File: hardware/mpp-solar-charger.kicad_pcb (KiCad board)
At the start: 2 copper layers, 136 parts, among them J101 Conn_01x04, J102 Conn_01x05, J103 Conn_01x05, Q201 Q_PNP_CBE, Q202 Q_PNP_CBE, Q203 Q_PNP_CBE, Q204 Q_PNP_CBE, Q205 Q_PNP_CBE, Q206 Q_NPN_CBE, Q207 Q_PNP_CBE, Q208 Q_PNP_CBE, Q209 Q_NPN_CBE, Q301 IRFZ48N, Q302 IRFZ48N, Q303 Q_PNP_CBE, Q304 BD135, Q305 BD136, Q306 Q_NPN_CBE, Q307 Q_PNP_CBE, Q308 Q_PNP_CBE, Q309 Q_NPN_CBE, Q310 Q_PNP_CBE, Q311 Q_PNP_CBE, Q312 Q_NPN_CBE, Q313 Q_NPN_CBE, U201 LP2950L-5.0, U202 LM324, U203 LM393

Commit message: Initial layout work
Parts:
- removed D305: D, Diodes_ThroughHole:D_DO-35_SOD27_P7.62mm_Horizontal
- D302: value D_Schottky -> MBR4045PT; footprint TO_SOT_Packages_THT:TO-220-2_Vertical -> TO_SOT_Packages_THT:TO-247_TO-3P_Vertical
- D303: value D_Schottky -> D_Zener; footprint TO_SOT_Packages_THT:TO-220-2_Vertical -> Diodes_ThroughHole:D_DO-41_SOD81_P7.62mm_Horizontal
- D304: value D_Zener -> D; footprint Diodes_ThroughHole:D_DO-41_SOD81_P7.62mm_Horizontal -> Diodes_ThroughHole:D_DO-35_SOD27_P7.62mm_Horizontal
- R306, R307: moved to B.Cu
- moved C301 131.7 mm to (278.8, 124.5), turned to 180 degrees
- moved C304 126.5 mm to (275.0, 104.1), turned to 270 degrees
- moved C313 117.7 mm to (262.9, 132.7), turned to 90 degrees
- moved Q209 115.7 mm to (36.0, 78.0)
- moved C212 114.7 mm to (34.0, 111.0)
- moved C211 113.9 mm to (36.0, 87.0)
- moved C205 113.5 mm to (38.0, 131.0)
- moved C208 112.0 mm to (37.0, 94.0)
- moved C302 111.6 mm to (259.7, 113.7), turned to 270 degrees
- moved Q206 111.5 mm to (38.0, 120.0)
- moved C306 111.2 mm to (259.7, 106.7)
- moved C207 109.5 mm to (39.0, 102.0)
- moved R244 108.7 mm to (53.0, 157.0)
- moved Q208 108.6 mm to (45.0, 72.0)
- moved R245 107.8 mm to (57.0, 162.0)
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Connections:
- D302 pad 1: Net-(C307-Pad2) -> GND
- D302 pad 2: GND -> Net-(C307-Pad2)
- D303 pad 1: Net-(C307-Pad2) -> Net-(D303-Pad1)
- D303 pad 2: GND -> Net-(C307-Pad2)
- D304 pad 1: Net-(D304-Pad1) -> Net-(C307-Pad2)
- D304 pad 2: Net-(C307-Pad2) -> Net-(D304-Pad2)
- Q306 pad 2: Net-(D304-Pad1) -> Net-(D303-Pad1)
- Q307 pad 2: Net-(D304-Pad1) -> Net-(D303-Pad1)
- Q310 pad 1: Net-(D304-Pad1) -> Net-(D303-Pad1)
- Q312 pad 3: Net-(D305-Pad2) -> Net-(D304-Pad2)
- Q313 pad 3: Net-(D305-Pad2) -> Net-(D304-Pad2)
- R308 pad 1: Net-(D304-Pad1) -> Net-(D303-Pad1)
- R312 pad 1: Net-(D304-Pad1) -> Net-(D303-Pad1)
- U202 pad 11: (no net) -> Net-(U202-Pad11)
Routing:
- net /Controller/VBAT: track 0.00 -> 70.1 mm
- net GND: track 0.00 -> 20.3 mm
- net Net-(L301-Pad2): track 0.00 -> 19.0 mm
- net Net-(Q303-Pad2): track 0.00 -> 13.4 mm
- net Net-(C309-Pad1): track 0.00 -> 10.3 mm
- net Net-(Q308-Pad3): track 0.00 -> 10.2 mm
- net /Controller/USENSE: track 0.00 -> 6.24 mm
- net Net-(Q303-Pad3): track 0.00 -> 3.59 mm
- net /Controller/UREF: track 0.00 -> 2.80 mm

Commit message: Layout work for power stage
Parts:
- moved Q209 228.3 mm to (264.3, 80.0), turned to 180 degrees
- moved U201 218.8 mm to (259.3, 130.8), turned to 180 degrees
- moved R244 215.4 mm to (267.8, 140.8)
- moved R237 215.2 mm to (267.8, 145.6)
- moved R242 214.8 mm to (267.8, 148.4)
- moved R236 213.0 mm to (267.8, 151.6)
- moved R246 200.1 mm to (257.0, 84.4)
- moved D304 189.8 mm to (263.0, 66.6), turned to 180 degrees
- moved U203 189.1 mm to (257.2, 140.7)
- moved C201 183.5 mm to (252.4, 132.6), turned to 90 degrees
- moved D207 175.0 mm to (267.8, 143.2)
- moved D201 174.0 mm to (251.0, 125.8)
- moved C202 172.9 mm to (263.8, 132.6), turned to 90 degrees
- moved R201 160.9 mm to (240.4, 125.4)
- moved Q312 103.2 mm to (250.2, 66.0)
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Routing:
- net GND: track 20.3 -> 215.1 mm, vias 0 -> 2
- net Net-(C307-Pad2): track 0.00 -> 157.6 mm, vias 0 -> 4
- net /Power-Stage/VSOLAR: track 0.00 -> 94.5 mm
- net Net-(C307-Pad1): track 0.00 -> 58.5 mm
- net Net-(D207-Pad1): track 0.00 -> 56.5 mm
- net /Controller/~SWITCH: track 0.00 -> 54.5 mm
- net Net-(D303-Pad1): track 0.00 -> 42.5 mm
- net Net-(Q301-Pad1): track 0.00 -> 32.1 mm
- net Net-(Q304-Pad3): track 0.00 -> 25.3 mm
- net Net-(Q313-Pad2): track 0.00 -> 20.8 mm
- net Net-(Q304-Pad1): track 0.00 -> 20.6 mm
- net Net-(D304-Pad2): track 0.00 -> 19.0 mm
- net Net-(C201-Pad1): track 0.00 -> 18.4 mm
- net Net-(Q302-Pad1): track 0.00 -> 13.7 mm
- net Net-(Q303-Pad2): track 13.4 -> 0.00 mm
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
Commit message: Layout work
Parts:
- R243: footprint Resistors_ThroughHole:R_Axial_DIN0207_L6.3mm_D2.5mm_P7.62mm_Horizontal -> Resistors_ThroughHole:R_Axial_DIN0207_L6.3mm_D2.5mm_P2.54mm_Vertical
- moved C211 222.5 mm to (255.1, 125.2), turned to 180 degrees
- moved Q206 213.2 mm to (251.1, 128.3), turned to 270 degrees
- moved C209 204.5 mm to (248.5, 112.3)
- moved Q205 203.0 mm to (251.1, 133.7), turned to 270 degrees
- moved Q208 190.0 mm to (225.4, 131.7), turned to 270 degrees
- moved Q204 188.9 mm to (239.0, 134.9), turned to 270 degrees
- moved R231 188.2 mm to (243.3, 124.7), turned to 270 degrees
- moved R230 183.8 mm to (243.3, 134.5), turned to 270 degrees
- moved R229 183.4 mm to (245.4, 111.8), turned to 270 degrees
- moved C207 182.8 mm to (221.8, 106.0), turned to 180 degrees
- moved C204 182.3 mm to (242.2, 101.6), turned to 270 degrees
- moved R228 180.9 mm to (255.4, 127.9), turned to 270 degrees
- moved C206 180.2 mm to (225.0, 99.4), turned to 180 degrees
- moved C208 179.7 mm to (213.4, 128.6), turned to 90 degrees
- moved R222 179.5 mm to (240.7, 140.5), turned to 180 degrees
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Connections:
- U202 pad 1: Net-(C206-Pad2) -> Net-(C210-Pad2)
- U202 pad 10: Net-(R240-Pad1) -> Net-(R220-Pad2)
- U202 pad 11: Net-(U202-Pad11) -> GND
- U202 pad 2: Net-(C207-Pad2) -> Net-(C208-Pad2)
- U202 pad 3: Net-(R220-Pad2) -> Net-(R209-Pad2)
- U202 pad 5: Net-(R209-Pad2) -> Net-(R240-Pad1)
- U202 pad 6: Net-(C208-Pad2) -> Net-(R235-Pad2)
- U202 pad 7: Net-(C210-Pad2) -> Net-(D205-Pad2)
- U202 pad 8: Net-(D205-Pad2) -> Net-(C206-Pad2)
- U202 pad 9: Net-(R235-Pad2) -> Net-(C207-Pad2)
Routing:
- net GND: track 215.1 -> 486.2 mm
- net /Controller/+5V: track 6.22 -> 147.6 mm
- net Net-(C208-Pad2): track 0.00 -> 53.5 mm
- net Net-(C205-Pad1): track 0.00 -> 45.3 mm
- net Net-(R234-Pad2): track 0.00 -> 39.9 mm
- net /Controller/VBAT: track 58.0 -> 93.8 mm
- net Net-(Q203-Pad1): track 0.00 -> 32.1 mm
- net Net-(C210-Pad2): track 0.00 -> 31.2 mm
- net Net-(D207-Pad1): track 56.5 -> 86.5 mm
- net /Controller/UMIN: track 0.00 -> 25.7 mm
- net Net-(Q203-Pad2): track 0.00 -> 25.7 mm
- net Net-(D203-Pad2): track 0.00 -> 25.5 mm, vias 0 -> 2
- net /Controller/UREG: track 0.00 -> 23.9 mm
- net Net-(C206-Pad2): track 0.00 -> 23.6 mm
- net /Controller/USAW: track 0.00 -> 21.3 mm
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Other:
- board outline added: 76.2 x 136.1 mm
- net class Default: clearance 0.2 -> 0.3
- rule trace_clearance: 0.2 -> 0.3

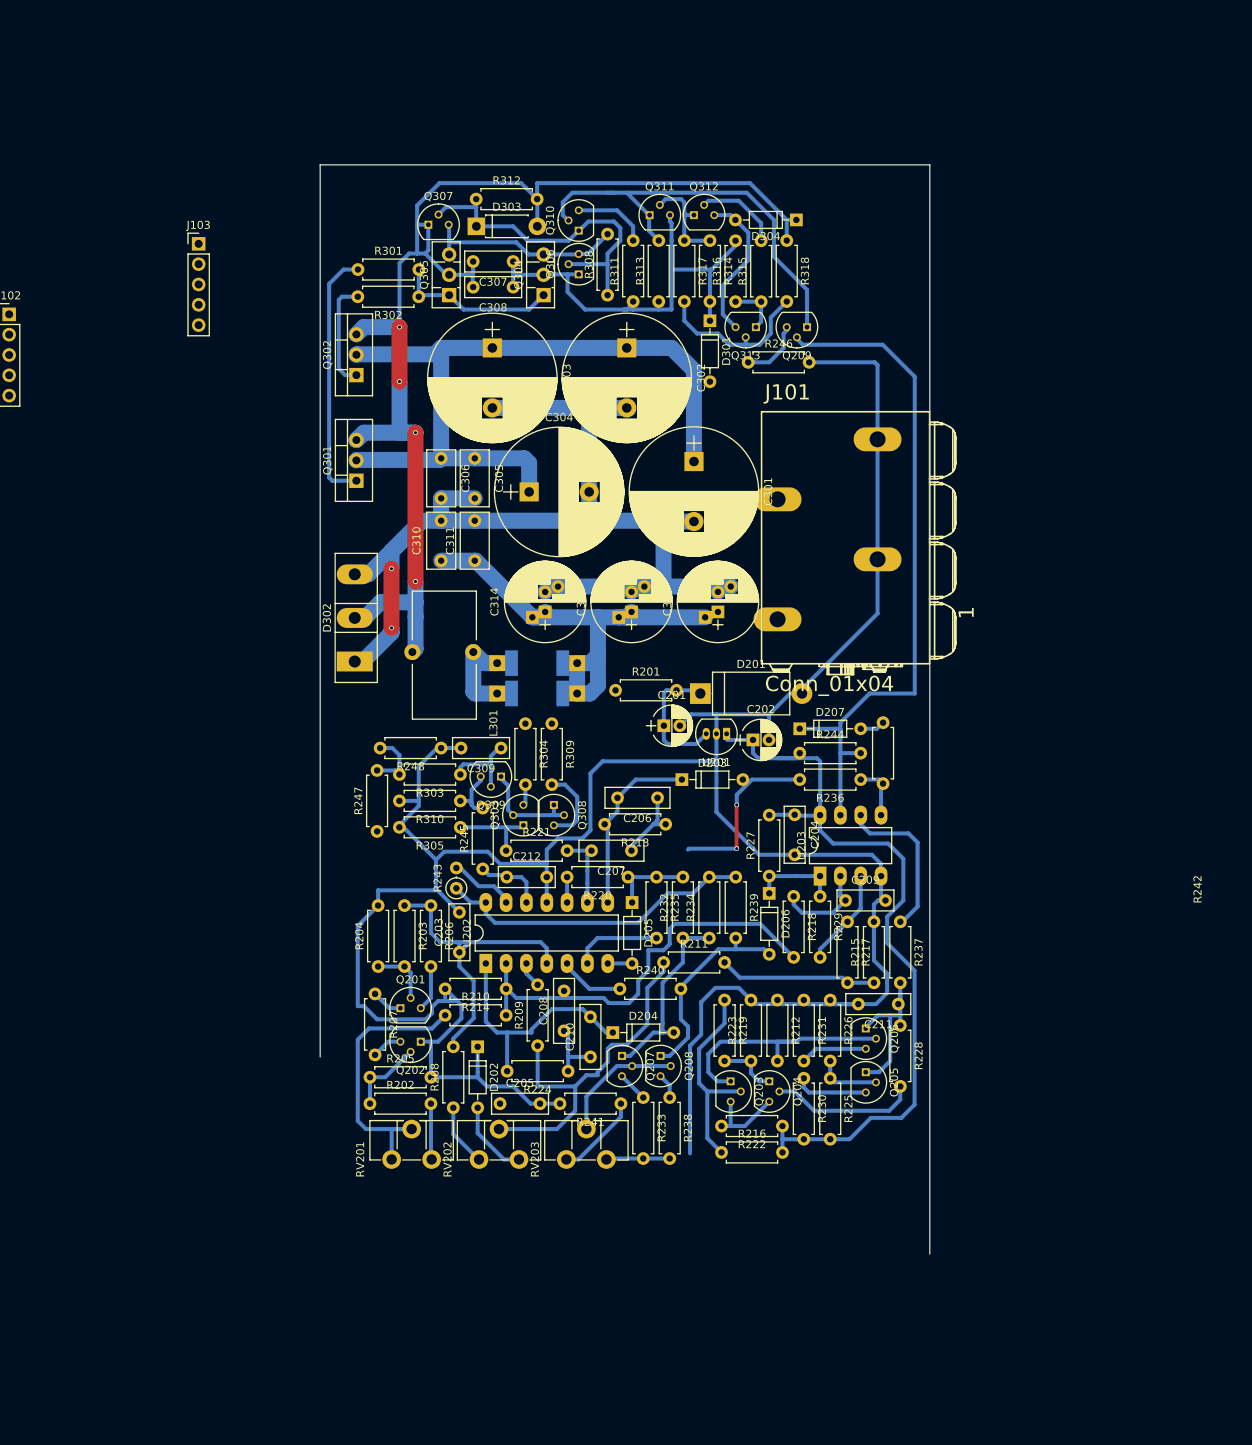
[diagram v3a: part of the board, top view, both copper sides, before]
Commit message: Condense layout
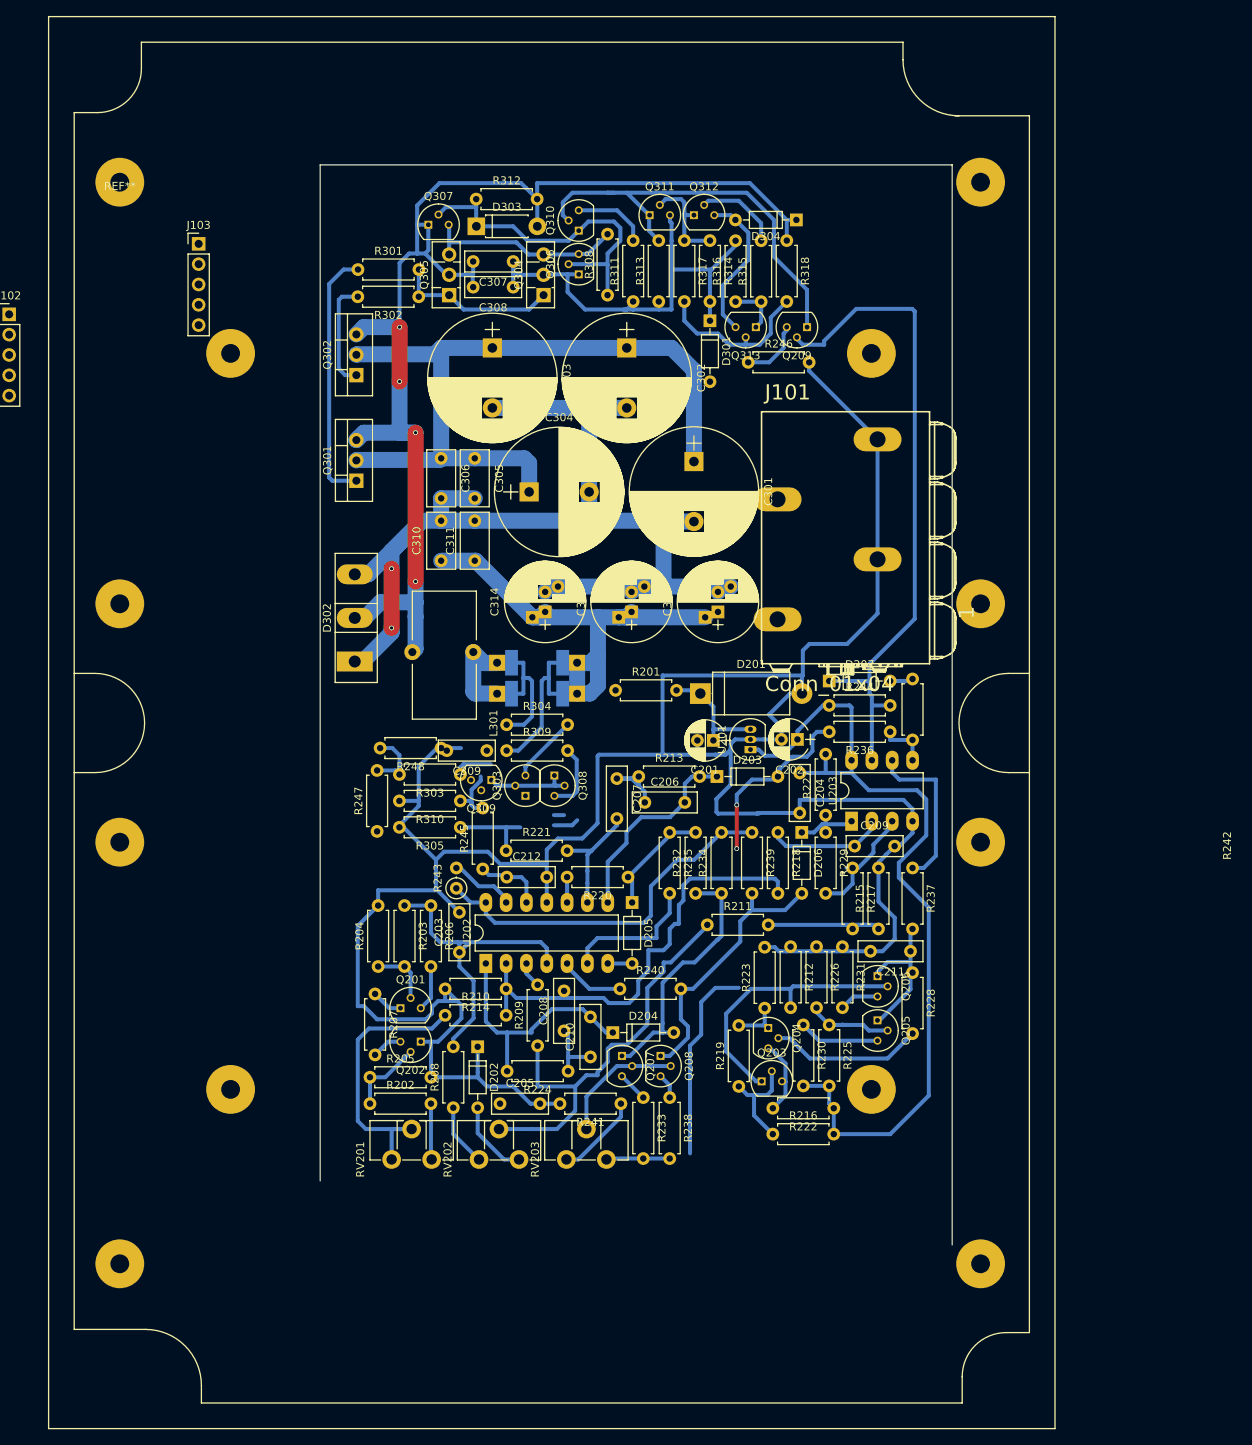
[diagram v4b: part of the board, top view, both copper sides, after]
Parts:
- added REF**: KRADEX_Z74, mpp-solar-charger:KRADEX_Z74, F.Cu at (157.8, 22.5)
- moved R219 10.9 mm to (235.2, 135.5), turned to 90 degrees
- moved R227 10.4 mm to (246.1, 101.6)
- moved C207 9.20 mm to (220.0, 97.0), turned to 270 degrees
- moved D206 8.64 mm to (243.1, 103.8)
- moved R218 8.24 mm to (240.1, 103.8)
- moved R231 8.23 mm to (248.2, 118.0)
- moved R229 8.03 mm to (246.1, 103.8)
- moved U203 7.91 mm to (249.3, 102.4)
- moved R211 7.20 mm to (231.3, 115.3)
- moved R236 7.01 mm to (254.1, 91.2)
- moved D207 7.01 mm to (246.5, 84.8)
- moved R244 7.01 mm to (246.5, 87.9)
- moved R237 6.90 mm to (256.9, 108.2)
- moved C209 6.89 mm to (249.7, 105.5)
- moved R226 6.88 mm to (244.9, 118.0)
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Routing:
- net /Controller/VBAT: track 93.8 -> 113.6 mm
- net Net-(L301-Pad2): track 11.6 -> 27.7 mm
- net GND: track 486.2 -> 501.8 mm
- net Net-(Q203-Pad2): track 25.7 -> 13.2 mm
- net /Controller/UMIN: track 25.7 -> 35.2 mm
- net /Controller/+5V: track 147.6 -> 156.2 mm
- net /Controller/UREG: track 23.9 -> 32.3 mm
- net Net-(C205-Pad1): track 45.3 -> 52.8 mm
- net Net-(R234-Pad2): track 39.9 -> 46.6 mm
- net Net-(R235-Pad2): track 11.1 -> 17.3 mm
- net Net-(Q303-Pad3): track 2.65 -> 8.53 mm
- net Net-(C309-Pad1): track 10.4 -> 4.86 mm
- net Net-(C207-Pad2): track 9.74 -> 15.1 mm
- net Net-(D205-Pad1): track 10.2 -> 14.4 mm
- net Net-(Q206-Pad3): track 8.38 -> 4.96 mm
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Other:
- board size 76.2 x 136.1 mm -> 79 x 135 mm

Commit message: Finish first revision of layout
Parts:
- removed the REF** at (157.8, 22.5)
- added REF**: COMBIPLAST_CP-11-26T, mpp-solar-charger:COMBIPLAST_CP-11-26T, F.Cu at (223.7, 68.8)
- D303: footprint Diodes_ThroughHole:D_DO-41_SOD81_P7.62mm_Horizontal -> Diodes_ThroughHole:D_DO-41_SOD81_P2.54mm_Vertical_AnodeUp
- R242, R312, R313: footprint Resistors_ThroughHole:R_Axial_DIN0207_L6.3mm_D2.5mm_P7.62mm_Horizontal -> Resistors_ThroughHole:R_Axial_DIN0207_L6.3mm_D2.5mm_P2.54mm_Vertical
- RV201, RV202, RV203: footprint Potentiometers:Potentiometer_Trimmer_Piher_PT-10h3.8_Vertical_Px3.8mm_Py5.0mm -> Potentiometers:Potentiometer_Trimmer_Piher_PT-6v_Horizontal
- moved J102 101.2 mm to (230.8, 91.2), turned to 270 degrees
- moved J103 87.5 mm to (192.7, 114.0), turned to 180 degrees
- moved Q209 46.1 mm to (257.2, 84.7), turned to 270 degrees
- moved R246 43.7 mm to (254.1, 85.0), turned to 180 degrees
- moved R203 27.1 mm to (189.1, 139.7), turned to 90 degrees
- moved D301 26.7 mm to (205.1, 36.6), turned to 180 degrees
- moved D303 25.1 mm to (227.3, 31.2)
- moved R317 22.6 mm to (249.9, 36.6), turned to 90 degrees
- moved R312 20.4 mm to (222.5, 27.7)
- moved R316 20.2 mm to (253.2, 29.0), turned to 270 degrees
- moved Q307 19.8 mm to (216.2, 28.7), turned to 180 degrees
- moved Q312 16.4 mm to (243.2, 35.8), turned to 90 degrees
- moved Q311 15.2 mm to (237.7, 33.3), turned to 270 degrees
- moved Q313 15.2 mm to (245.5, 27.7), turned to 270 degrees
- moved RV201 13.7 mm to (201.5, 135.0), turned to 180 degrees
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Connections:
- J101 pad 1: /Power-Stage/VSOLAR -> /Controller/VBAT
- J101 pad 3: /Controller/VBAT -> /Power-Stage/VSOLAR
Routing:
- net /Controller/+5V: track 156.2 -> 278.2 mm, vias 0 -> 6
- net /Power-Stage/VSOLAR: track 94.5 -> 209.6 mm, vias 0 -> 4
- net /Controller/VBAT: track 113.6 -> 213.6 mm, vias 0 -> 4
- net Net-(D203-Pad2): track 27.2 -> 80.9 mm, vias 2 -> 4
- net Net-(D207-Pad1): track 83.4 -> 29.7 mm
- net /Controller/CHARGED: track 8.96 -> 47.9 mm, vias 0 -> 2
- net /Controller/~SWITCH: track 54.5 -> 87.1 mm, vias 0 -> 2
- net Net-(C307-Pad1): track 58.5 -> 84.1 mm
- net Net-(Q313-Pad1): track 6.65 -> 25.1 mm
- net Net-(D303-Pad1): track 42.5 -> 24.4 mm
- net Net-(C307-Pad2): track 157.6 -> 140.6 mm
- net /Controller/USENSE: track 10.4 -> 26.1 mm
- net Net-(Q204-Pad2): track 19.1 -> 4.18 mm
- net /Controller/USAW: track 18.6 -> 32.7 mm
- net Net-(D304-Pad2): track 19.0 -> 6.12 mm
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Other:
- board size 79 x 135 mm -> 79 x 132 mm
- net class Default: via_dia 0.6 -> 1.4; via_drill 0.4 -> 0.8

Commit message: Finalize & validate layout
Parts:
- moved D206 2.04 mm to (242.7, 111.1)
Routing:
- net GND: track 491.5 -> 522.9 mm, vias 6 -> 8
- net Net-(R236-Pad1): track 5.72 -> 8.80 mm
- net /Controller/CHARGED: track 47.9 -> 45.2 mm
- net /Power-Stage/VSOLAR: track 209.6 -> 211.3 mm
- net Net-(Q301-Pad1): track 32.1 -> 30.5 mm
- net Net-(C309-Pad1): track 12.0 -> 13.6 mm
- net Net-(C307-Pad1): track 84.1 -> 82.7 mm
- net Net-(C205-Pad1): track 46.9 -> 48.3 mm
- net Net-(Q203-Pad3): track 14.8 -> 16.1 mm
- net /Controller/UMIN: track 31.3 -> 30.3 mm
- net Net-(R208-Pad1): track 4.66 -> 3.69 mm
- net Net-(Q304-Pad3): track 28.8 -> 29.8 mm
- net Net-(Q302-Pad1): track 13.7 -> 12.7 mm
- net /Controller/VBAT: track 213.6 -> 214.6 mm
- net Net-(C206-Pad2): track 18.5 -> 19.2 mm
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- added copper zone on B.Cu, net /Controller/VBAT
- added copper zone on B.Cu, net /Power-Stage/VSOLAR
- added copper zone on B.Cu, net GND
- added copper zone on B.Cu, net Net-(C307-Pad2)
- added copper zone on B.Cu, net Net-(L301-Pad2)

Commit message: Finalization of hardware
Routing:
- net /Controller/+5V: track 278.1 -> 282.6 mm
- net /Controller/VBAT: track 214.6 -> 212.6 mm
- net Net-(L301-Pad2): track 31.3 -> 29.6 mm
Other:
- board size 79 x 132 mm -> 79 x 121 mm
- board text added: "MPP Charger rev1 A. Messer 2018"
